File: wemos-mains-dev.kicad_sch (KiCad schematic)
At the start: 15 parts, among them J1 Screw_Terminal_01x02, J2 Conn_01x08, J3 Conn_01x08, J8 SDA PU, J9 SDA PU, U1 AC-05-3, U2 WeMos_D1_mini

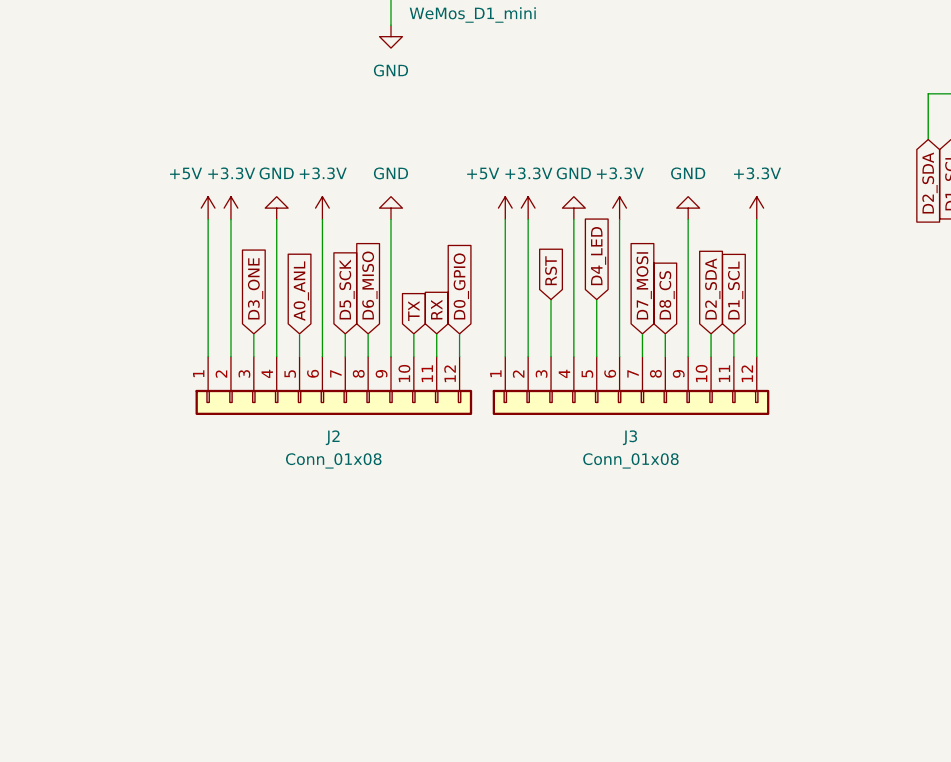
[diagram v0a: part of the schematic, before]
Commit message: Changed pinheader for breakout to 02x12
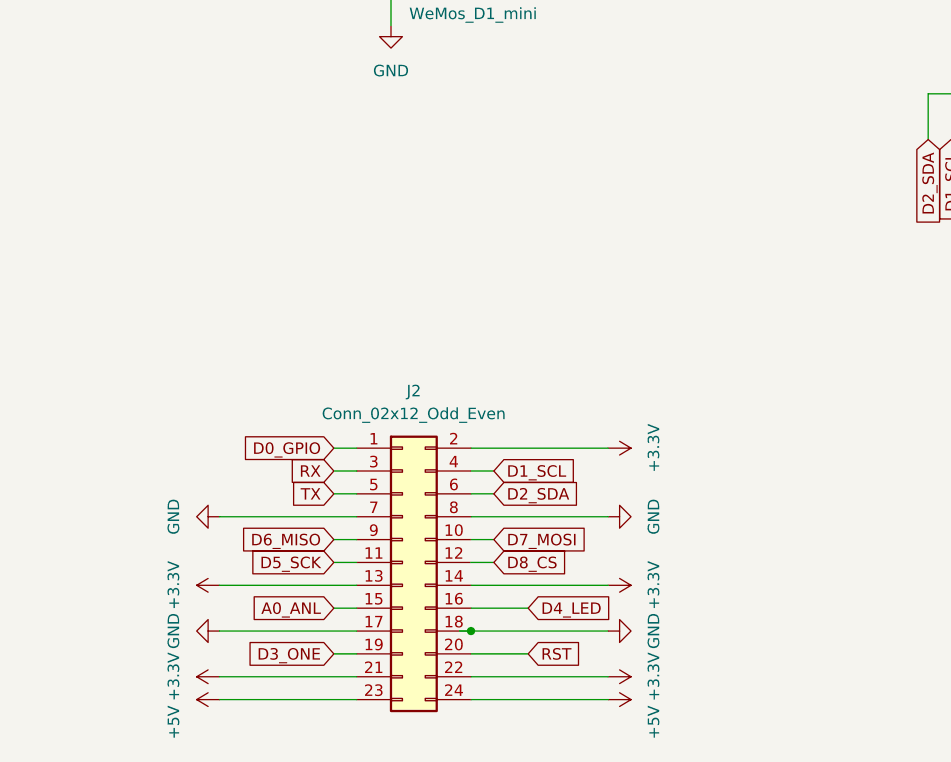
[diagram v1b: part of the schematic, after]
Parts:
- removed J2, J3: Conn_01x08, Connector_PinHeader_2.54mm:PinHeader_1x12_P2.54mm_Vertical, symbol Connector_Generic:Conn_01x12
- added J2: Conn_02x12_Odd_Even, Connector_PinHeader_2.54mm:PinHeader_2x12_P2.54mm_Vertical, symbol Connector_Generic:Conn_02x12_Odd_Even
- H1, H2, H3, H4: footprint (none) -> MountingHole:MountingHole_3.2mm_M3-smallBorder
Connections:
- net +3V3: now also J2.13 (Pin_13), J2.14 (Pin_14), J2.2 (Pin_2), J2.21 (Pin_21), J2.22 (Pin_22)
- net +5V: now also J2.23 (Pin_23), J2.24 (Pin_24)
- net A0_ANL: now also J2.15 (Pin_15)
- net D0_GPIO: now also J2.1 (Pin_1)
- net D1_SCL: now also J2.4 (Pin_4)
- net D2_SDA: now also J2.6 (Pin_6)
- net D3_ONE: now also J2.19 (Pin_19)
- net D4_LED: now also J2.16 (Pin_16)
- net D5_SCK: now also J2.11 (Pin_11)
- net D6_MISO: now also J2.9 (Pin_9)
- net D7_MOSI: now also J2.10 (Pin_10)
- net D8_CS: now also J2.12 (Pin_12)
- net GND: now also J2.17 (Pin_17), J2.18 (Pin_18), J2.7 (Pin_7), J2.8 (Pin_8)
- net RST: now also J2.20 (Pin_20)
- net RX: now also J2.3 (Pin_3)
- net TX: now also J2.5 (Pin_5)

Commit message: Updated template for KiCAD 7
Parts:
- U1: symbol Converter_ACDC:AC-05-3 -> Chof747 Voltage Regulators:AC-05-3
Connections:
- net +3V3 renamed +3.3V

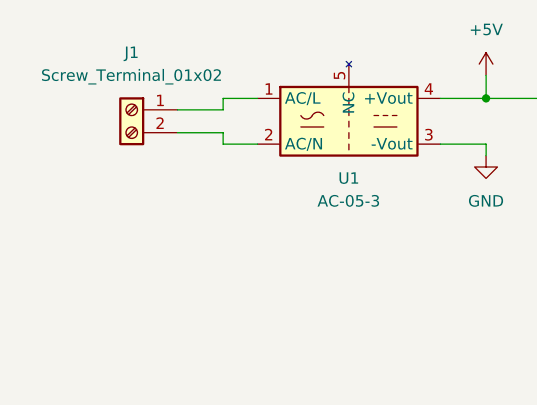
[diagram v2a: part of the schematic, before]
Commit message: Corrections for rev. 1
- Corrected orientation of power supply footprint
- Reduced ground plane to low voltage side
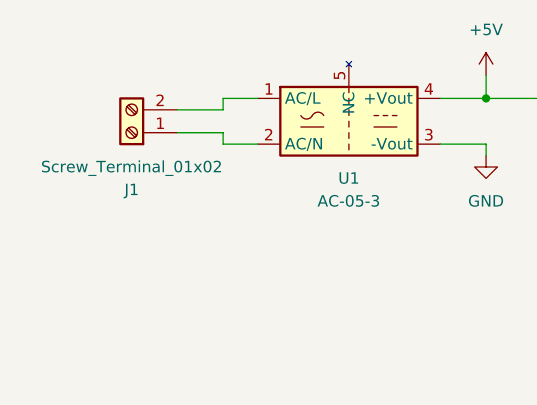
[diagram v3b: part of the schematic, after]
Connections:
- net at J1.1 (Pin_1): now also U1.2 (AC/N); no longer U1.1 (AC/L)
- net at J1.2 (Pin_2): now also U1.1 (AC/L); no longer U1.2 (AC/N)
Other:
- moved on the sheet: J1
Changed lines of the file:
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@@
-    (stroke (width 0) (type default))
-  )
-  (wire (pts (xy 34.29 40.64) (xy 29.21 40.64))
     (stroke (width 0) (type default))
   )
@@
   )
   (wire (pts (xy 116.84 62.23) (xy 121.92 62.23))
+    (stroke (width 0) (type default))
+  )
+  (wire (pts (xy 29.21 40.64) (xy 34.29 40.64))
     (stroke (width 0) (type default))
   )
@@
     )
   )
-  (symbol (lib_id "Connector:Screw_Terminal_01x02") (at 24.13 40.64 0) (mirror y) (unit 1)
-    (in_bom yes) (on_board yes) (dnp no) (fields_autoplaced)
-    (property "Reference" "J1" (at 24.13 34.29 0)
-      (effects (font (size 1.27 1.27)))
-    )
-    (property "Value" "Screw_Terminal_01x02" (at 24.13 36.83 0)
-      (effects (font (size 1.27 1.27)))
-    )
-    (property "Footprint" "TerminalBlock:TerminalBlock_bornier-2_P5.08mm" (at 24.13 40.64 0)
-      (effects (font (size 1.27 1.27)) hide)
-    )
-    (property "Datasheet" "~" (at 24.13 40.64 0)
-      (effects (font (size 1.27 1.27)) hide)
-    )
+  (symbol (lib_id "Connector:Screw_Terminal_01x02") (at 24.13 43.18 180) (unit 1)
+    (in_bom yes) (on_board yes) (dnp no)
+    (property "Reference" "J1" (at 24.13 49.53 0)
+      (effects (font (size 1.27 1.27)))
+    )
+    (property "Value" "Screw_Terminal_01x02" (at 24.13 46.99 0)
+      (effects (font (size 1.27 1.27)))
+    )
+    (property "Footprint" "TerminalBlock:TerminalBlock_bornier-2_P5.08mm" (at 24.13 43.18 0)
+      (effects (font (size 1.27 1.27)) hide)
+    )
+    (property "Datasheet" "~" (at 24.13 43.18 0)
+      (effects (font (size 1.27 1.27)) hide)
+    )

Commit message: changed hat socket to socket from header
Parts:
- J2: footprint Connector_PinHeader_2.54mm:PinHeader_2x12_P2.54mm_Vertical -> Connector_PinSocket_2.54mm:PinSocket_2x12_P2.54mm_Vertical
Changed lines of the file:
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@@
       (effects (font (size 1.27 1.27)))
     )
-    (property "Footprint" "Connector_PinHeader_2.54mm:PinHeader_2x12_P2.54mm_Vertical" (at 107.95 151.13 0)
+    (property "Footprint" "Connector_PinSocket_2.54mm:PinSocket_2x12_P2.54mm_Vertical" (at 107.95 151.13 0)
       (effects (font (size 1.27 1.27)) hide)
     )
